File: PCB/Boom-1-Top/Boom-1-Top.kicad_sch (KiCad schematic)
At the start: 1029 parts, among them J1 DEBUG, J10 PIC_DEBUG, J11 PIC_DEBUG, J12 PIC_DEBUG, J13 PIC_DEBUG, J14 PIC_DEBUG, J15 USB_B_Micro, J16 SD_Card, J17 BT_DEBUG, J18 12V Supply, J19 3V3 Bypass, J2 MIDI IN, J20 5V Bypass, J21 Env +12V Supply, J22 Env -12V Supply, J23 OLEDConn, J24 FiltConn1PassThru, J25 LeftI2C0Test, J26 AudioOutConn, J27 FiltConn2PassThru, J28 FiltConn2PassThruPower, J29 LeftI2C1Test, J3 MIDI OUT, J30 LeftI2C2Test, J31 LeftI2C3Test, J32 RightI2C0Test, J33 RightI2C1Test, J34 RightI2C2Test, J35 RightI2C3Test, J36 SPIBus1Test, J37 Osc1Conn, J38 Osc2Conn, J39 SubNoiseConn, J4 PIC_DEBUG, J40 FiltConn2, J41 EnvGenConn2, J42 EnvGenConn1, J43 FXConn1, J44 FiltConn1, J45 FXConn2, J46 EnvGenConn3, J47 BTTestConn, J48 MIDITestConn, J49 I2CBus1TestConn, J5 PIC_DEBUG, J50 I2CBus2TestConn, J51 OLEDTestConn, J52 SDIOTestConn, J53 HapticEngine, J54 OLEDPowerTest, J6 PIC_DEBUG, J7 PIC_DEBUG, J8 PIC_DEBUG, J9 PIC_DEBUG, Q1 AO3401A, Q2 AO3401A, SW1 Osc1SawEncoder, SW10 SubToOsc2FiltEncoder, SW11 Osc1ToOsc2FiltEncoder, SW12 Osc1FiltFreqEncoder, SW13 Osc2FiltFreqEncoder, SW14 SubFiltFreqEncoder, SW15 OscFiltEnvAttackEncoder, SW16 SubFiltEnvAttackEncoder, SW17 Osc1FiltResEncoder, SW18 Osc2FiltResEncoder, SW19 SubFiltResEncoder, SW2 Osc1SqrEncoder, SW20 OscFiltEnvDecayEncoder, SW21 SubFiltEnvDecayEncoder, SW22 OscFiltEnvSustainEncoder, SW23 SubFiltEnvSustainEncoder, SW24 Osc1DriveEncoder, SW25 Osc2DistortionEncoder, SW26 OscFiltEnvReleaseEncoder, SW27 SubFiltEnvReleaseEncoder, SW28 FXWetDryEncoder, SW29 SubAmpEnvAttackEncoder, SW3 Rotary_Encoder, SW30 OscAmpEnvAttackEncoder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

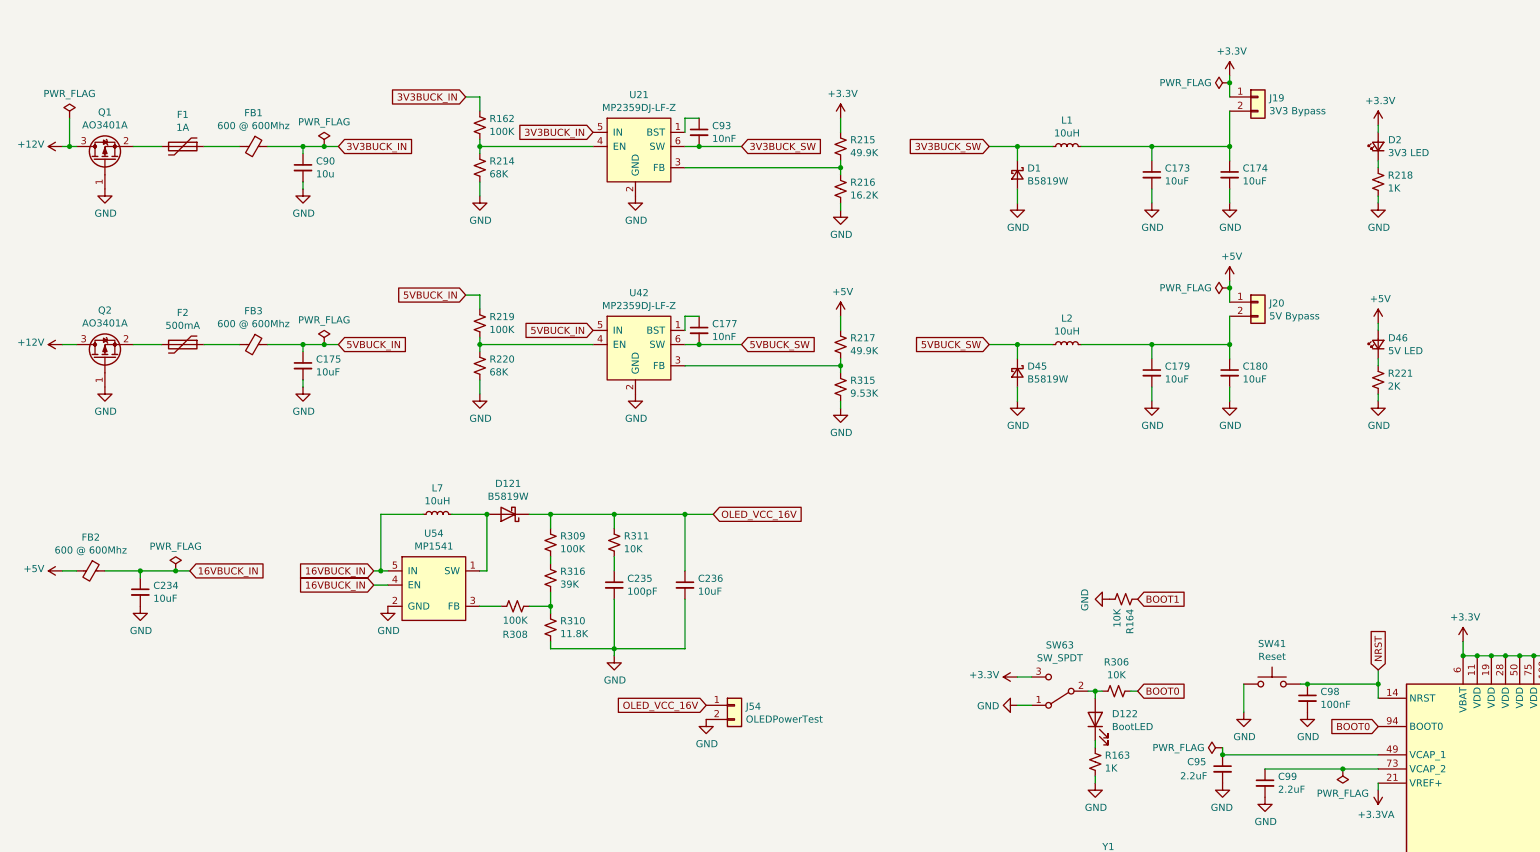
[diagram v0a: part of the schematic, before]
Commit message: Top: Power Rails
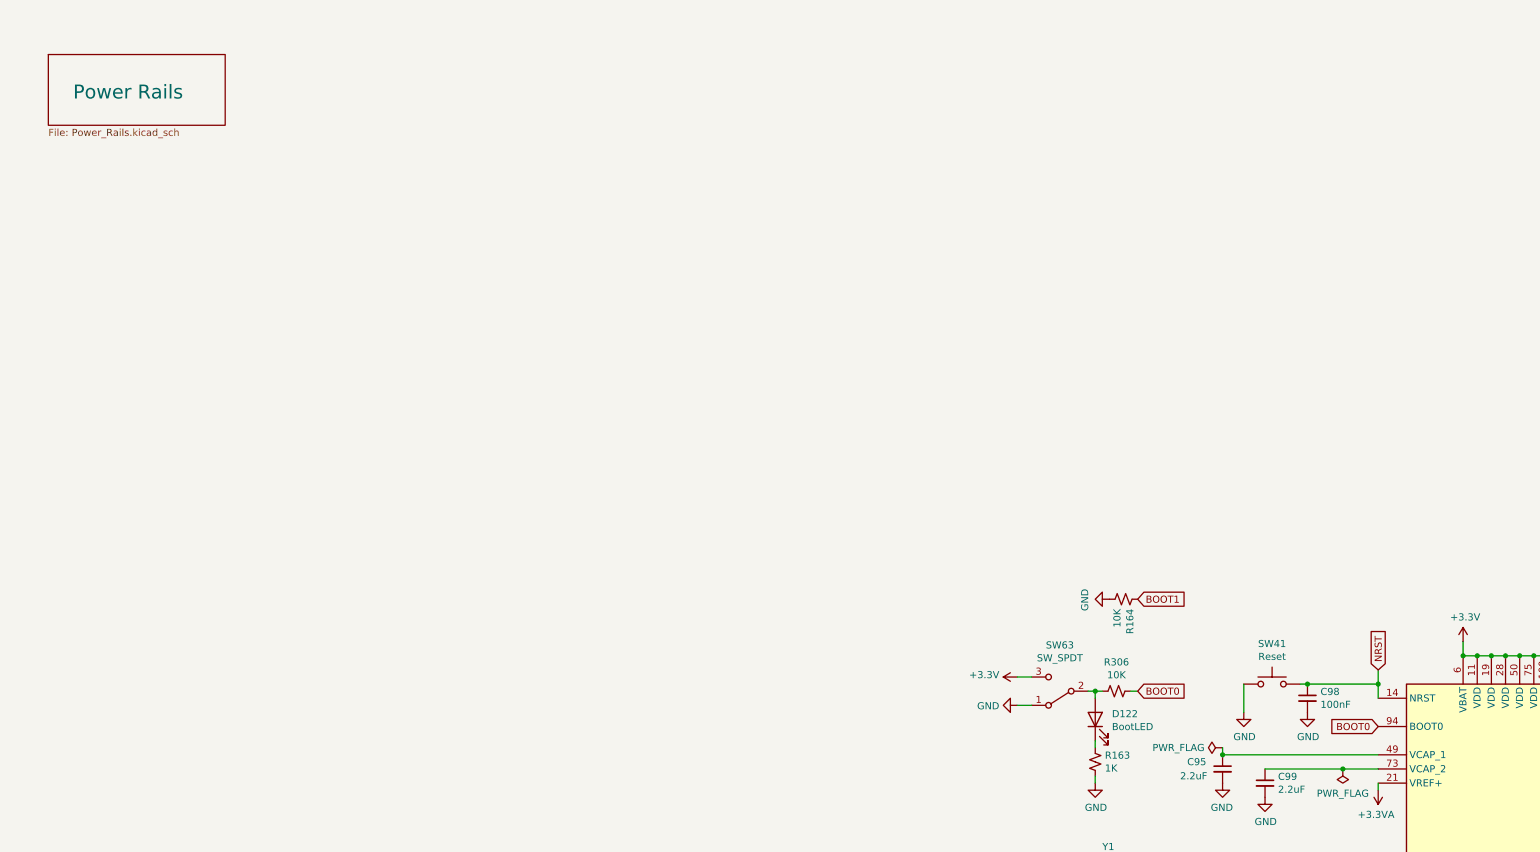
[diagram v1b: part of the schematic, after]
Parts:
- removed C173, C174, C175, C179, C180, C234, C236: 10uF, Capacitor_SMD:C_1206_3216Metric, symbol Device:C_Small
- removed C177, C93: 10nF, Capacitor_SMD:C_0805_2012Metric, symbol Device:C_Small
- removed C235: 100pF, Capacitor_SMD:C_0805_2012Metric, symbol Device:C_Small
- removed C90: 10u, Capacitor_SMD:C_1206_3216Metric, symbol Device:C_Small
- removed D1, D45: B5819W, Diode_SMD:D_SOD-123, symbol Device:D_Schottky_Small
- removed D121: B5819W, Diode_SMD:D_SOD-123, symbol Device:D_Schottky
- removed D2: 3V3 LED, LED_SMD:LED_0603_1608Metric, symbol Device:LED_Small
- removed D46: 5V LED, LED_SMD:LED_0603_1608Metric, symbol Device:LED_Small
- removed F1: 1A, Fuse:Fuse_1206_3216Metric, symbol Device:Polyfuse
- removed F2: 500mA, Fuse:Fuse_1206_3216Metric, symbol Device:Polyfuse
- removed FB1, FB2, FB3: 600 @ 600Mhz, Inductor_SMD:L_0805_2012Metric, symbol Device:Ferrite_Bead_Small
- removed J19: 3V3 Bypass, TerminalBlock:TerminalBlock_bornier-2_P5.08mm, symbol Connector_Generic:Conn_01x02
- removed J20: 5V Bypass, TerminalBlock:TerminalBlock_bornier-2_P5.08mm, symbol Connector_Generic:Conn_01x02
- removed J54: OLEDPowerTest, Connector_PinSocket_2.54mm:PinSocket_1x02_P2.54mm_Vertical, symbol Connector_Generic:Conn_01x02
- removed L1, L2, L7: 10uH, Inductor_SMD:L_Sunlord_MWSA0518_5.4x5.2mm, symbol Device:L_Small
- removed Q1, Q2: AO3401A, Package_TO_SOT_SMD:SOT-23, symbol Transistor_FET:AO3401A
- removed R162, R219, R308: 100K, Resistor_SMD:R_1206_3216Metric, symbol Device:R_Small_US
- removed R214, R220: 68K, Resistor_SMD:R_0603_1608Metric, symbol Device:R_Small_US
- removed R215, R217: 49.9K, Resistor_SMD:R_0603_1608Metric, symbol Device:R_Small_US
- removed R216: 16.2K, Resistor_SMD:R_0603_1608Metric, symbol Device:R_Small_US
- removed R218: 1K, Resistor_SMD:R_0603_1608Metric, symbol Device:R_Small_US
- removed R221: 2K, Resistor_SMD:R_0603_1608Metric, symbol Device:R_Small_US
- removed R309: 100K, Resistor_SMD:R_0805_2012Metric, symbol Device:R_Small_US
- removed R310: 11.8K, Resistor_SMD:R_1206_3216Metric, symbol Device:R_Small_US
- removed R311: 10K, Resistor_SMD:R_1206_3216Metric, symbol Device:R_Small_US
- removed R315: 9.53K, Resistor_SMD:R_0603_1608Metric, symbol Device:R_Small_US
- removed R316: 39K, Resistor_SMD:R_0805_2012Metric, symbol Device:R_Small_US
- removed U21, U42: MP2359DJ-LF-Z, Package_TO_SOT_SMD:SOT-23-6, symbol MP2359DJ:MP2359DJ-LF-Z
- removed U54: MP1541, Package_TO_SOT_SMD:TSOT-23-5, symbol MP1541:MP1541
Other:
- added sheet Power Rails (Power_Rails.kicad_sch)

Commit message: Top: Mounting
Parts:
- removed H1, H10, H11, H12, H2, H3, H4, H5, H6, H8: MountingHole_Pad, MountingHole:MountingHole_2.2mm_M2_Pad, symbol Mechanical:MountingHole_Pad
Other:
- added sheet Mounting (Mounting.kicad_sch)

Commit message: Top: SD IO
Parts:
- removed J16: SD_Card, Connector_Card:SD_Kyocera_145638009211859+, symbol Connector:SD_Card
- removed J52: SDIOTestConn, Connector_PinHeader_2.54mm:PinHeader_2x06_P2.54mm_Vertical, symbol Connector_Generic:Conn_02x06_Odd_Even
- removed R206, R207, R208, R209, R210: 47K, Resistor_SMD:R_0603_1608Metric, symbol Device:R_Small_US
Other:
- added sheet SD IO (SD_IO.kicad_sch)

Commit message: Top [WIP]: Rotary Encoders
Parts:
- removed C1, C10, C11, C12, C13, C139, C14, C140, C19, C2, C20, C21, C22, C23, C24, C25, C26, C27, C28, C29, C3, C30, C31, C32, C33, C34, C35, C36, C37, C38, C39, C4, C40, C41, C42, C43, C44, C45, C46, C47, C48, C49, C5, C50, C51, C52, C53, C54, C55, C56, C57, C58, C59, C6, C60, C61, C62, C63, C64, C65, C66, C67, C68, C69, C7, C70, C71, C72, C73, C74, C75, C76, C77, C78, C79, C8, C80, C9: 47nF, Capacitor_SMD:C_0603_1608Metric, symbol Device:C_Small
- removed C117, C118, C119, C120, C121, C122, C123, C124, C125, C126, C127, C128, C129, C130, C131, C132, C133, C134, C135, C136, C137, C138: 100nF, Capacitor_SMD:C_0402_1005Metric, symbol Device:C_Small
- removed D11, D14, D15, D17, D19, D23, D24, D25, D5, D6, D7, D9: B5819W, Diode_SMD:D_SOD-123, symbol Device:D_Small
- removed D12: Osc1SqrMixLED, LED_SMD:LED_0603_1608Metric, symbol Device:LED
- removed D13: Osc1SqrPWMLED, LED_SMD:LED_0603_1608Metric, symbol Device:LED
- removed D16: Osc2SqrMixLED, LED_SMD:LED_0603_1608Metric, symbol Device:LED
- removed D18: Osc2SqrPWMLED, LED_SMD:LED_0603_1608Metric, symbol Device:LED
- removed D43: OscFiltEnv1LED, LED_SMD:LED_0603_1608Metric, symbol Device:LED
- removed D44: OscFiltEnv2LED, LED_SMD:LED_0603_1608Metric, symbol Device:LED
- removed D52: OscFiltSusLED, LED_SMD:LED_0603_1608Metric, symbol Device:LED
- removed D53: OscFiltAmtLED, LED_SMD:LED_0603_1608Metric, symbol Device:LED
- removed D54: SubFilt1LED, LED_SMD:LED_0603_1608Metric, symbol Device:LED
- removed D55: SubFilt2LED, LED_SMD:LED_0603_1608Metric, symbol Device:LED
- removed D58: SubFiltSusLED, LED_SMD:LED_0603_1608Metric, symbol Device:LED
- removed D59: SubFiltAmtLED, LED_SMD:LED_0603_1608Metric, symbol Device:LED
- removed D62: OscAmpEnvSusLED, LED_SMD:LED_0603_1608Metric, symbol Device:LED
- removed D63: OscAmpEnvAmtLED, LED_SMD:LED_0603_1608Metric, symbol Device:LED
- removed D64: SubAmpEnvSusLED, LED_SMD:LED_0603_1608Metric, symbol Device:LED
- removed D65: SubAmpEnvAmtLED, LED_SMD:LED_0603_1608Metric, symbol Device:LED
- removed J10, J11, J12, J13, J14, J4, J5, J6, J7, J8, J9: PIC_DEBUG, Connector_PinHeader_1.27mm:PinHeader_1x05_P1.27mm_Vertical, symbol Connector_Generic:Conn_01x05
- removed R1, R10, R100, R101, R102, R103, R104, R105, R106, R107, R108, R109, R11, R110, R111, R112, R113, R114, R115, R116, R117, R118, R119, R12, R120, R121, R122, R123, R124, R125, R126, R127, R128, R129, R13, R130, R131, R132, R133, R134, R135, R136, R137, R138, R139, R14, R140, R141, R142, R143, R144, R145, R146, R147, R148, R149, R15, R150, R151, R152, R153, R154, R155, R156, R157, R158, R159, R16, R160, R17, R18, R183, R184, R185, R186, R2, R21, R22, R23, R24, R27, R28, R29, R3, R30, R31, R32, R37, R38, R39, R4, R40, R41, R42, R43, R44, R45, R46, R47, R48, R49, R5, R50, R51, R52, R53, R54, R55, R56, R57, R58, R59, R6, R60, R61, R62, R63, R64, R65, R66, R67, R68, R69, R7, R70, R71, R72, R73, R74, R75, R76, R77, R78, R79, R8, R80, R81, R82, R83, R84, R85, R86, R87, R88, R89, R9, R90, R91, R92, R93, R94, R95, R96, R97, R98, R99: 10K, Resistor_SMD:R_0402_1005Metric, symbol Device:R_Small_US
- removed R172, R173, R174, R175, R176, R177, R178, R179, R180, R181, R182: 10K, Resistor_SMD:R_0603_1608Metric, symbol Device:R_Small_US
- removed R276, R277, R278, R279, R280, R281, R282, R283, R284, R285, R286, R287, R288, R289, R290, R291: 42R2, Resistor_SMD:R_0603_1608Metric, symbol Device:R_Small_US
- removed SW1: Osc1SawEncoder, PEC11R:PEC11R-4x15F-N0024, symbol Device:Rotary_Encoder
- removed SW10: SubToOsc2FiltEncoder, PEC11R:PEC11R-4x15F-N0024, symbol Device:Rotary_Encoder
- removed SW11: Osc1ToOsc2FiltEncoder, PEC11R:PEC11R-4x15F-N0024, symbol Device:Rotary_Encoder
- removed SW12: Osc1FiltFreqEncoder, PEC11R:PEC11R-4x15F-N0024, symbol Device:Rotary_Encoder
- removed SW13: Osc2FiltFreqEncoder, PEC11R:PEC11R-4x15F-N0024, symbol Device:Rotary_Encoder
- removed SW14: SubFiltFreqEncoder, PEC11R:PEC11R-4x15F-N0024, symbol Device:Rotary_Encoder
- removed SW15: OscFiltEnvAttackEncoder, PEC11R:PEC11R-4x15F-S0024, symbol Device:Rotary_Encoder_Switch
- removed SW16: SubFiltEnvAttackEncoder, PEC11R:PEC11R-4x15F-S0024, symbol Device:Rotary_Encoder_Switch
- removed SW17: Osc1FiltResEncoder, PEC11R:PEC11R-4x15F-N0024, symbol Device:Rotary_Encoder
- removed SW18: Osc2FiltResEncoder, PEC11R:PEC11R-4x15F-N0024, symbol Device:Rotary_Encoder
- removed SW19: SubFiltResEncoder, PEC11R:PEC11R-4x15F-N0024, symbol Device:Rotary_Encoder
- removed SW2: Osc1SqrEncoder, PEC11R:PEC11R-4x15F-S0024, symbol Device:Rotary_Encoder_Switch
- removed SW20: OscFiltEnvDecayEncoder, PEC11R:PEC11R-4x15F-N0024, symbol Device:Rotary_Encoder
- removed SW21: SubFiltEnvDecayEncoder, PEC11R:PEC11R-4x15F-N0024, symbol Device:Rotary_Encoder
- removed SW22: OscFiltEnvSustainEncoder, PEC11R:PEC11R-4x15F-S0024, symbol Device:Rotary_Encoder_Switch
- removed SW23: SubFiltEnvSustainEncoder, PEC11R:PEC11R-4x15F-S0024, symbol Device:Rotary_Encoder_Switch
- removed SW24: Osc1DriveEncoder, PEC11R:PEC11R-4x15F-N0024, symbol Device:Rotary_Encoder
- removed SW25: Osc2DistortionEncoder, PEC11R:PEC11R-4x15F-N0024, symbol Device:Rotary_Encoder
- removed SW26: OscFiltEnvReleaseEncoder, PEC11R:PEC11R-4x15F-N0024, symbol Device:Rotary_Encoder
- removed SW27: SubFiltEnvReleaseEncoder, PEC11R:PEC11R-4x15F-N0024, symbol Device:Rotary_Encoder
- removed SW28: FXWetDryEncoder, PEC11R:PEC11R-4x15F-S0024, symbol Device:Rotary_Encoder_Switch
- removed SW29: SubAmpEnvAttackEncoder, PEC11R:PEC11R-4x15F-N0024, symbol Device:Rotary_Encoder
- removed SW3, SW5: Rotary_Encoder, PEC11R:PEC11R-4x15F-N0024, symbol Device:Rotary_Encoder
- removed SW30: OscAmpEnvAttackEncoder, PEC11R:PEC11R-4x15F-N0024, symbol Device:Rotary_Encoder
- removed SW31: FXControl1Encoder, PEC11R:PEC11R-4x15F-N0024, symbol Device:Rotary_Encoder
- removed SW32: SubAmpEnvDecayEncoder, PEC11R:PEC11R-4x15F-N0024, symbol Device:Rotary_Encoder
- removed SW33: OscAmpEnvDecayEncoder, PEC11R:PEC11R-4x15F-N0024, symbol Device:Rotary_Encoder
- removed SW34: FXControl2Encoder, PEC11R:PEC11R-4x15F-N0024, symbol Device:Rotary_Encoder
- removed SW35: SubAmpEnvSustainEncoder, PEC11R:PEC11R-4x15F-S0024, symbol Device:Rotary_Encoder_Switch
- removed SW36: OscAmpEnvSustainEncoder, PEC11R:PEC11R-4x15F-S0024, symbol Device:Rotary_Encoder_Switch
- removed SW37: FXControl3Encoder, PEC11R:PEC11R-4x15F-N0024, symbol Device:Rotary_Encoder
- removed SW38: FXFeedbackEncoder, PEC11R:PEC11R-4x15F-N0024, symbol Device:Rotary_Encoder
- removed SW39: SubAmpEnvReleaseEncoder, PEC11R:PEC11R-4x15F-N0024, symbol Device:Rotary_Encoder
- removed SW4: Rotary_Encoder_Switch, PEC11R:PEC11R-4x15F-S0024, symbol Device:Rotary_Encoder_Switch
- removed SW40: OscAmpEnvReleaseEncoder, PEC11R:PEC11R-4x15F-N0024, symbol Device:Rotary_Encoder
- removed SW43: Reset, PTS636:PTS636, symbol Switch:SW_Push
- removed SW53: Osc1TuneEncoder, PEC11R:PEC11R-4x15F-S0024, symbol Device:Rotary_Encoder_Switch
- removed SW6: SubToSubFiltEncoder, PEC11R:PEC11R-4x15F-N0024, symbol Device:Rotary_Encoder
- removed SW7: SubNoiseEncoder, PEC11R:PEC11R-4x15F-N0024, symbol Device:Rotary_Encoder
- removed U11, U12, U13, U14, U15, U16, U17, U18, U19, U2, U20: PIC18F26Q43, Package_SO:SSOP-28_5.3x10.2mm_P0.65mm, symbol PIC18F26Q43:PIC18F26Q43
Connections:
- no-connect marks 334 -> 262
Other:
- added sheet Rotary Encoders (Rotary_Encoders.kicad_sch)
- note removed: "GND"
- note removed: "LEFT0:000"
- note removed: "LEFT0:001"
- note removed: "LEFT0:010"
- note removed: "LEFT0:011"
- note removed: "LEFT0:100"
- note removed: "LEFT2:000"
- note removed: "LEFT2:001"
- note removed: "LEFT3:000"
- note removed: "PGC"
- note removed: "PGD"
- note removed: "RIGHT0:000"
- note removed: "RIGHT1:000"
- note removed: "RIGHT1:001"
- note removed: "VDD"
- note removed: "VPP/MCLR"

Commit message: Top: more splitting up done, still [WIP]
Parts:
- removed C100, C101, C141, C143, C145, C147, C149, C15, C150, C151, C153, C154, C155, C156, C157, C158, C160, C162, C164, C165, C168, C169, C17, C171, C172, C187, C195, C203, C209, C213, C215, C216, C217, C218, C219, C221, C222, C224, C225, C226, C227, C229, C81, C83, C87, C89, C91, C92, C94, C96, C98: 100nF, Capacitor_SMD:C_0402_1005Metric, symbol Device:C_Small
- removed C102, C82, C84, C97: 10uF, Capacitor_SMD:C_0603_1608Metric, symbol Device:CP_Small
- removed C142, C144, C146, C148, C152, C159, C16, C161, C163, C166, C167, C18, C188, C196, C204, C210, C214, C220, C223: 1uF, Capacitor_SMD:C_0402_1005Metric, symbol Device:C_Small
- removed C170: 10nF, Capacitor_SMD:C_0402_1005Metric, symbol Device:C_Small
- removed C228, C86: 4.7uF, Capacitor_SMD:C_0805_2012Metric, symbol Device:C_Small
- removed C85, C88: 12pF, Capacitor_SMD:C_0402_1005Metric, symbol Device:C_Small
- removed C95, C99: 2.2uF, Capacitor_SMD:C_0603_1608Metric, symbol Device:C_Small
- removed D100: OscTuneLED11, LED_SMD:LED_0603_1608Metric, symbol Device:LED
- removed D101: OscTuneLED12, LED_SMD:LED_0603_1608Metric, symbol Device:LED
- removed D102: OscTuneLED13, LED_SMD:LED_0603_1608Metric, symbol Device:LED
- removed D103: Osc2FiltLED1, fm-b2020rgba-hg:FM-B2020RGBA-HG, symbol fm-b2020rgba-hg:FM-B2020RGBA-HG
- removed D104: Osc2FiltLED2, fm-b2020rgba-hg:FM-B2020RGBA-HG, symbol fm-b2020rgba-hg:FM-B2020RGBA-HG
- removed D105, D106, D109, D110, D68, D69, D72, D73, D74, D75, D80, D81, D82, D83, D84, D85, D88, D89: StepLED, fm-b2020rgba-hg:FM-B2020RGBA-HG, symbol fm-b2020rgba-hg:FM-B2020RGBA-HG
- removed D107: SubFiltLED1, fm-b2020rgba-hg:FM-B2020RGBA-HG, symbol fm-b2020rgba-hg:FM-B2020RGBA-HG
- removed D108: SubFiltLED2, fm-b2020rgba-hg:FM-B2020RGBA-HG, symbol fm-b2020rgba-hg:FM-B2020RGBA-HG
- removed D111: OscFiltEnvLED1, fm-b2020rgba-hg:FM-B2020RGBA-HG, symbol fm-b2020rgba-hg:FM-B2020RGBA-HG
- removed D112: OscFiltEnvLED2, fm-b2020rgba-hg:FM-B2020RGBA-HG, symbol fm-b2020rgba-hg:FM-B2020RGBA-HG
- removed D113: OscFiltEnvLED3, fm-b2020rgba-hg:FM-B2020RGBA-HG, symbol fm-b2020rgba-hg:FM-B2020RGBA-HG
- removed D114, D115, D116, D120: PageLED, LED_SMD:LED_0603_1608Metric, symbol Device:LED
- removed D117: SubFiltEnvLED1, fm-b2020rgba-hg:FM-B2020RGBA-HG, symbol fm-b2020rgba-hg:FM-B2020RGBA-HG
- removed D118: SubFiltEnvLED2, fm-b2020rgba-hg:FM-B2020RGBA-HG, symbol fm-b2020rgba-hg:FM-B2020RGBA-HG
- removed D119: SubFiltEnvLED3, fm-b2020rgba-hg:FM-B2020RGBA-HG, symbol fm-b2020rgba-hg:FM-B2020RGBA-HG
- removed D122: BootLED, LED_SMD:LED_0603_1608Metric, symbol Device:LED
- removed D123: Osc1ResLED1, fm-b2020rgba-hg:FM-B2020RGBA-HG, symbol fm-b2020rgba-hg:FM-B2020RGBA-HG
- removed D124: Osc1ResLED2, fm-b2020rgba-hg:FM-B2020RGBA-HG, symbol fm-b2020rgba-hg:FM-B2020RGBA-HG
- removed D127: Osc2ResLED1, fm-b2020rgba-hg:FM-B2020RGBA-HG, symbol fm-b2020rgba-hg:FM-B2020RGBA-HG
- removed D128: Osc2ResLED2, fm-b2020rgba-hg:FM-B2020RGBA-HG, symbol fm-b2020rgba-hg:FM-B2020RGBA-HG
- removed D131: SubResLED1, fm-b2020rgba-hg:FM-B2020RGBA-HG, symbol fm-b2020rgba-hg:FM-B2020RGBA-HG
- removed D132: SubResLED2, fm-b2020rgba-hg:FM-B2020RGBA-HG, symbol fm-b2020rgba-hg:FM-B2020RGBA-HG
- removed D133: SubResLED3, fm-b2020rgba-hg:FM-B2020RGBA-HG, symbol fm-b2020rgba-hg:FM-B2020RGBA-HG
- removed D134: SubResLED4, fm-b2020rgba-hg:FM-B2020RGBA-HG, symbol fm-b2020rgba-hg:FM-B2020RGBA-HG
- removed D135: SubResLED5, fm-b2020rgba-hg:FM-B2020RGBA-HG, symbol fm-b2020rgba-hg:FM-B2020RGBA-HG
- removed D136: SubResLED6, fm-b2020rgba-hg:FM-B2020RGBA-HG, symbol fm-b2020rgba-hg:FM-B2020RGBA-HG
- removed D137: SubResLED7, fm-b2020rgba-hg:FM-B2020RGBA-HG, symbol fm-b2020rgba-hg:FM-B2020RGBA-HG
- removed D144: Osc1DriveLED1, fm-b2020rgba-hg:FM-B2020RGBA-HG, symbol fm-b2020rgba-hg:FM-B2020RGBA-HG
- removed D145: Osc1DriveLED2, fm-b2020rgba-hg:FM-B2020RGBA-HG, symbol fm-b2020rgba-hg:FM-B2020RGBA-HG
- removed D147: Osc1DriveLED3, fm-b2020rgba-hg:FM-B2020RGBA-HG, symbol fm-b2020rgba-hg:FM-B2020RGBA-HG
- removed D148: Osc1DriveLED4, fm-b2020rgba-hg:FM-B2020RGBA-HG, symbol fm-b2020rgba-hg:FM-B2020RGBA-HG
- removed D152: Osc2DriveLED2, fm-b2020rgba-hg:FM-B2020RGBA-HG, symbol fm-b2020rgba-hg:FM-B2020RGBA-HG
- removed D153: Osc2DriveLED10, fm-b2020rgba-hg:FM-B2020RGBA-HG, symbol fm-b2020rgba-hg:FM-B2020RGBA-HG
- removed D154: Osc2DriveLED3, fm-b2020rgba-hg:FM-B2020RGBA-HG, symbol fm-b2020rgba-hg:FM-B2020RGBA-HG
- removed D159: Osc2DriveLED13, fm-b2020rgba-hg:FM-B2020RGBA-HG, symbol fm-b2020rgba-hg:FM-B2020RGBA-HG
- removed D162: OscAmpLED1, fm-b2020rgba-hg:FM-B2020RGBA-HG, symbol fm-b2020rgba-hg:FM-B2020RGBA-HG
- removed D163: OscAmpLED2, fm-b2020rgba-hg:FM-B2020RGBA-HG, symbol fm-b2020rgba-hg:FM-B2020RGBA-HG
- removed D164: OscAmpLED3, fm-b2020rgba-hg:FM-B2020RGBA-HG, symbol fm-b2020rgba-hg:FM-B2020RGBA-HG
- removed D165: SubAmpLED1, fm-b2020rgba-hg:FM-B2020RGBA-HG, symbol fm-b2020rgba-hg:FM-B2020RGBA-HG
- removed D166: SubAmpLED2, fm-b2020rgba-hg:FM-B2020RGBA-HG, symbol fm-b2020rgba-hg:FM-B2020RGBA-HG
- removed D167: SubAmpLED3, fm-b2020rgba-hg:FM-B2020RGBA-HG, symbol fm-b2020rgba-hg:FM-B2020RGBA-HG
- removed D168: SubAmpLED4, fm-b2020rgba-hg:FM-B2020RGBA-HG, symbol fm-b2020rgba-hg:FM-B2020RGBA-HG
- removed D169: SubvAmpLED5, fm-b2020rgba-hg:FM-B2020RGBA-HG, symbol fm-b2020rgba-hg:FM-B2020RGBA-HG
- removed D173: OscAmpLED4, fm-b2020rgba-hg:FM-B2020RGBA-HG, symbol fm-b2020rgba-hg:FM-B2020RGBA-HG
- removed D174: OscAmpLED5, fm-b2020rgba-hg:FM-B2020RGBA-HG, symbol fm-b2020rgba-hg:FM-B2020RGBA-HG
- removed D175: FXDryLED1, fm-b2020rgba-hg:FM-B2020RGBA-HG, symbol fm-b2020rgba-hg:FM-B2020RGBA-HG
- removed D176: FXDryLED2, fm-b2020rgba-hg:FM-B2020RGBA-HG, symbol fm-b2020rgba-hg:FM-B2020RGBA-HG
- removed D177: FXDryLED3, fm-b2020rgba-hg:FM-B2020RGBA-HG, symbol fm-b2020rgba-hg:FM-B2020RGBA-HG
- removed D178: FXDryLED4, fm-b2020rgba-hg:FM-B2020RGBA-HG, symbol fm-b2020rgba-hg:FM-B2020RGBA-HG
- removed D179: FXDryLED5, fm-b2020rgba-hg:FM-B2020RGBA-HG, symbol fm-b2020rgba-hg:FM-B2020RGBA-HG
- removed D180: FXDryLED6, fm-b2020rgba-hg:FM-B2020RGBA-HG, symbol fm-b2020rgba-hg:FM-B2020RGBA-HG
- removed D181: FXDryLED7, fm-b2020rgba-hg:FM-B2020RGBA-HG, symbol fm-b2020rgba-hg:FM-B2020RGBA-HG
- removed D182: FXDryLED8, fm-b2020rgba-hg:FM-B2020RGBA-HG, symbol fm-b2020rgba-hg:FM-B2020RGBA-HG
- removed D183: FXDryLED9, fm-b2020rgba-hg:FM-B2020RGBA-HG, symbol fm-b2020rgba-hg:FM-B2020RGBA-HG
- removed D184: FXDryLED10, fm-b2020rgba-hg:FM-B2020RGBA-HG, symbol fm-b2020rgba-hg:FM-B2020RGBA-HG
- removed D190: FXWetLED1, fm-b2020rgba-hg:FM-B2020RGBA-HG, symbol fm-b2020rgba-hg:FM-B2020RGBA-HG
- removed D193: FXWetLED4, fm-b2020rgba-hg:FM-B2020RGBA-HG, symbol fm-b2020rgba-hg:FM-B2020RGBA-HG
- removed D196: FXWetLED7, fm-b2020rgba-hg:FM-B2020RGBA-HG, symbol fm-b2020rgba-hg:FM-B2020RGBA-HG
- removed D197: FXWetLED8, fm-b2020rgba-hg:FM-B2020RGBA-HG, symbol fm-b2020rgba-hg:FM-B2020RGBA-HG
- removed D198: FXWetLED9, fm-b2020rgba-hg:FM-B2020RGBA-HG, symbol fm-b2020rgba-hg:FM-B2020RGBA-HG
- removed D199: FXWetLED10, fm-b2020rgba-hg:FM-B2020RGBA-HG, symbol fm-b2020rgba-hg:FM-B2020RGBA-HG
- removed D20: Osc1SawLED2, fm-b2020rgba-hg:FM-B2020RGBA-HG, symbol fm-b2020rgba-hg:FM-B2020RGBA-HG
- removed D202: FXFbLED1, fm-b2020rgba-hg:FM-B2020RGBA-HG, symbol fm-b2020rgba-hg:FM-B2020RGBA-HG
- removed D203: FXFbLED2, fm-b2020rgba-hg:FM-B2020RGBA-HG, symbol fm-b2020rgba-hg:FM-B2020RGBA-HG
- removed D205: FXFbLED3, fm-b2020rgba-hg:FM-B2020RGBA-HG, symbol fm-b2020rgba-hg:FM-B2020RGBA-HG
- removed D206: FXFbLED4, fm-b2020rgba-hg:FM-B2020RGBA-HG, symbol fm-b2020rgba-hg:FM-B2020RGBA-HG
- removed D207: FXFbLED5, fm-b2020rgba-hg:FM-B2020RGBA-HG, symbol fm-b2020rgba-hg:FM-B2020RGBA-HG
- removed D209: FXFbLED6, fm-b2020rgba-hg:FM-B2020RGBA-HG, symbol fm-b2020rgba-hg:FM-B2020RGBA-HG
- removed D21: Osc1SqrLED2, fm-b2020rgba-hg:FM-B2020RGBA-HG, symbol fm-b2020rgba-hg:FM-B2020RGBA-HG
- removed D210: FXFbLED7, fm-b2020rgba-hg:FM-B2020RGBA-HG, symbol fm-b2020rgba-hg:FM-B2020RGBA-HG
- removed D211: FXFbLED18, fm-b2020rgba-hg:FM-B2020RGBA-HG, symbol fm-b2020rgba-hg:FM-B2020RGBA-HG
- removed D218: OscFiltEnvAtkLED1, LED_SMD:LED_0603_1608Metric, symbol Device:LED
- removed D219: OscFiltEnvAtkLED2, LED_SMD:LED_0603_1608Metric, symbol Device:LED
- removed D22: Osc2SawLED2, fm-b2020rgba-hg:FM-B2020RGBA-HG, symbol fm-b2020rgba-hg:FM-B2020RGBA-HG
- removed D220: OscFiltEnvAtkLED3, LED_SMD:LED_0603_1608Metric, symbol Device:LED
- removed D221: OscFiltEnvAtkLED4, LED_SMD:LED_0603_1608Metric, symbol Device:LED
- removed D222: OscFiltEnvAtkLED5, LED_SMD:LED_0603_1608Metric, symbol Device:LED
- removed D223: OscFiltEnvAtkLED6, LED_SMD:LED_0603_1608Metric, symbol Device:LED
- removed D224: OscFiltEnvDcyLED1, LED_SMD:LED_0603_1608Metric, symbol Device:LED
- removed D225: OscFiltEnvDcyLED2, LED_SMD:LED_0603_1608Metric, symbol Device:LED
- removed D226: OscFiltEnvDcyLED3, LED_SMD:LED_0603_1608Metric, symbol Device:LED
- removed D227: OscFiltEnvDcyLED4, LED_SMD:LED_0603_1608Metric, symbol Device:LED
- removed D228: OscFiltEnvDcyLED5, LED_SMD:LED_0603_1608Metric, symbol Device:LED
- removed D229: OscFiltEnvDcyLED6, LED_SMD:LED_0603_1608Metric, symbol Device:LED
- removed D230: OscFiltEnvSusLED1, LED_SMD:LED_0603_1608Metric, symbol Device:LED
- removed D231: OscFiltEnvSusLED2, LED_SMD:LED_0603_1608Metric, symbol Device:LED
- removed D232: OscFiltEnvSusLED3, LED_SMD:LED_0603_1608Metric, symbol Device:LED
- removed D233: OscFiltEnvSusLED4, LED_SMD:LED_0603_1608Metric, symbol Device:LED
- removed D234: OscFiltEnvSusLED5, LED_SMD:LED_0603_1608Metric, symbol Device:LED
- removed D235: OscFiltEnvSusLED6, LED_SMD:LED_0603_1608Metric, symbol Device:LED
- removed D236: OscFiltEnvRelLED1, LED_SMD:LED_0603_1608Metric, symbol Device:LED
- removed D237: OscFiltEnvRelLED2, LED_SMD:LED_0603_1608Metric, symbol Device:LED
- removed D238: OscFiltEnvRelLED3, LED_SMD:LED_0603_1608Metric, symbol Device:LED
- removed D239: OscFiltEnvRelLED4, LED_SMD:LED_0603_1608Metric, symbol Device:LED
- removed D240: OscFiltEnvRelLED5, LED_SMD:LED_0603_1608Metric, symbol Device:LED
- removed D241: OscFiltEnvRelLED6, LED_SMD:LED_0603_1608Metric, symbol Device:LED
- removed D242: SubFiltEnvAtkLED1, LED_SMD:LED_0603_1608Metric, symbol Device:LED
- removed D243: SubFiltEnvAtkLED2, LED_SMD:LED_0603_1608Metric, symbol Device:LED
- removed D244: SubFiltEnvAtkLED3, LED_SMD:LED_0603_1608Metric, symbol Device:LED
- removed D245: SubFiltEnvAtkLED4, LED_SMD:LED_0603_1608Metric, symbol Device:LED
- removed D246: SubFiltEnvAtkLED5, LED_SMD:LED_0603_1608Metric, symbol Device:LED
- removed D247: SubFiltEnvAtkLED6, LED_SMD:LED_0603_1608Metric, symbol Device:LED
- removed D248: SubFiltEnvDcyLED1, LED_SMD:LED_0603_1608Metric, symbol Device:LED
- removed D249: SubFiltEnvDcyLED2, LED_SMD:LED_0603_1608Metric, symbol Device:LED
- removed D250: SubFiltEnvDcyLED3, LED_SMD:LED_0603_1608Metric, symbol Device:LED
- removed D251: SubFiltEnvDcyLED4, LED_SMD:LED_0603_1608Metric, symbol Device:LED
- removed D252: SubFiltEnvDcyLED5, LED_SMD:LED_0603_1608Metric, symbol Device:LED
- removed D253: SubFiltEnvDcyLED6, LED_SMD:LED_0603_1608Metric, symbol Device:LED
- removed D254: SubFiltEnvSusLED1, LED_SMD:LED_0603_1608Metric, symbol Device:LED
- removed D255: SubFiltEnvSusLED2, LED_SMD:LED_0603_1608Metric, symbol Device:LED
- removed D256: SubFiltEnvSusLED3, LED_SMD:LED_0603_1608Metric, symbol Device:LED
- removed D257: SubFiltEnvSusLED4, LED_SMD:LED_0603_1608Metric, symbol Device:LED
- removed D258: SubFiltEnvSusLED5, LED_SMD:LED_0603_1608Metric, symbol Device:LED
- removed D259: SubFiltEnvSusLED6, LED_SMD:LED_0603_1608Metric, symbol Device:LED
- removed D26: Osc2NoiseLED2, fm-b2020rgba-hg:FM-B2020RGBA-HG, symbol fm-b2020rgba-hg:FM-B2020RGBA-HG
- removed D260: SubFiltEnvRelLED1, LED_SMD:LED_0603_1608Metric, symbol Device:LED
- removed D261: SubFiltEnvRelLED2, LED_SMD:LED_0603_1608Metric, symbol Device:LED
- removed D262: SubFiltEnvRelLED3, LED_SMD:LED_0603_1608Metric, symbol Device:LED
- removed D263: SubFiltEnvRelLED4, LED_SMD:LED_0603_1608Metric, symbol Device:LED
- removed D264: SubFiltEnvRelLED5, LED_SMD:LED_0603_1608Metric, symbol Device:LED
- removed D265: SubFiltEnvRelLED6, LED_SMD:LED_0603_1608Metric, symbol Device:LED
- removed D266: OscAmpEnvAtkLED1, LED_SMD:LED_0603_1608Metric, symbol Device:LED
- removed D267: OscAmpEnvAtkLED2, LED_SMD:LED_0603_1608Metric, symbol Device:LED
- removed D268: OscAmpEnvAtkLED3, LED_SMD:LED_0603_1608Metric, symbol Device:LED
- removed D269: OscAmpEnvAtkLED4, LED_SMD:LED_0603_1608Metric, symbol Device:LED
- removed D27: SubOscLED2, fm-b2020rgba-hg:FM-B2020RGBA-HG, symbol fm-b2020rgba-hg:FM-B2020RGBA-HG
- removed D270: OscAmpEnvAtkLED5, LED_SMD:LED_0603_1608Metric, symbol Device:LED
- removed D271: OscAmpEnvAtkLED6, LED_SMD:LED_0603_1608Metric, symbol Device:LED
- removed D272: OscAmpEnvDcyLED1, LED_SMD:LED_0603_1608Metric, symbol Device:LED
- removed D273: OscAmpEnvDcyLED2, LED_SMD:LED_0603_1608Metric, symbol Device:LED
- removed D274: OscAmpEnvDcyLED3, LED_SMD:LED_0603_1608Metric, symbol Device:LED
- removed D275: OscAmpEnvDcyLED4, LED_SMD:LED_0603_1608Metric, symbol Device:LED
- removed D276: OscAmpEnvDcyLED5, LED_SMD:LED_0603_1608Metric, symbol Device:LED
- removed D277: OscAmpEnvDcyLED6, LED_SMD:LED_0603_1608Metric, symbol Device:LED
- removed D278: OscAmpEnvSusLED1, LED_SMD:LED_0603_1608Metric, symbol Device:LED
- removed D279: OscAmpEnvSusLED2, LED_SMD:LED_0603_1608Metric, symbol Device:LED
- removed D28: SubNoiseLED2, fm-b2020rgba-hg:FM-B2020RGBA-HG, symbol fm-b2020rgba-hg:FM-B2020RGBA-HG
- removed D280: OscAmpEnvSusLED3, LED_SMD:LED_0603_1608Metric, symbol Device:LED
- removed D281: OscAmpEnvSusLED4, LED_SMD:LED_0603_1608Metric, symbol Device:LED
- removed D282: OscAmpEnvSusLED5, LED_SMD:LED_0603_1608Metric, symbol Device:LED
- removed D283: OscAmpEnvSusLED6, LED_SMD:LED_0603_1608Metric, symbol Device:LED
- removed D284: OscAmpEnvRelLED1, LED_SMD:LED_0603_1608Metric, symbol Device:LED
- removed D285: OscAmpEnvRelLED2, LED_SMD:LED_0603_1608Metric, symbol Device:LED
- removed D286: OscAmpEnvRelLED3, LED_SMD:LED_0603_1608Metric, symbol Device:LED
- removed D287: OscAmpEnvRelLED4, LED_SMD:LED_0603_1608Metric, symbol Device:LED
- removed D288: OscAmpEnvRelLED5, LED_SMD:LED_0603_1608Metric, symbol Device:LED
- removed D289: OscAmpEnvRelLED6, LED_SMD:LED_0603_1608Metric, symbol Device:LED
- removed D29: Osc2SqrLED2, fm-b2020rgba-hg:FM-B2020RGBA-HG, symbol fm-b2020rgba-hg:FM-B2020RGBA-HG
- removed D290: SubAmpEnvAtkLED1, LED_SMD:LED_0603_1608Metric, symbol Device:LED
- removed D291: SubAmpEnvAtkLED2, LED_SMD:LED_0603_1608Metric, symbol Device:LED
- removed D292: SubAmpEnvAtkLED3, LED_SMD:LED_0603_1608Metric, symbol Device:LED
- removed D293: SubAmpEnvAtkLED4, LED_SMD:LED_0603_1608Metric, symbol Device:LED
- removed D294: SubAmpEnvAtkLED5, LED_SMD:LED_0603_1608Metric, symbol Device:LED
- removed D295: SubAmpEnvAtkLED6, LED_SMD:LED_0603_1608Metric, symbol Device:LED
- removed D296: SubAmpEnvDcyLED1, LED_SMD:LED_0603_1608Metric, symbol Device:LED
- removed D297: SubAmpEnvDcyLED2, LED_SMD:LED_0603_1608Metric, symbol Device:LED
- removed D298: SubAmpEnvDcyLED3, LED_SMD:LED_0603_1608Metric, symbol Device:LED
- removed D299: SubAmpEnvDcyLED4, LED_SMD:LED_0603_1608Metric, symbol Device:LED
- removed D3: 1N4148, Diode_SMD:D_SOD-123, symbol Device:D_Small
- removed D30: Osc1SawLED3, fm-b2020rgba-hg:FM-B2020RGBA-HG, symbol fm-b2020rgba-hg:FM-B2020RGBA-HG
- removed D300: SubAmpEnvDcyLED5, LED_SMD:LED_0603_1608Metric, symbol Device:LED
- removed D301: SubAmpEnvDcyLED6, LED_SMD:LED_0603_1608Metric, symbol Device:LED
- removed D302: SubAmpEnvSusLED1, LED_SMD:LED_0603_1608Metric, symbol Device:LED
- removed D303: SubAmpEnvSusLED2, LED_SMD:LED_0603_1608Metric, symbol Device:LED
- removed D304: SubAmpEnvSusLED3, LED_SMD:LED_0603_1608Metric, symbol Device:LED
- removed D305: SubAmpEnvSusLED4, LED_SMD:LED_0603_1608Metric, symbol Device:LED
- removed D306: SubAmpEnvSusLED5, LED_SMD:LED_0603_1608Metric, symbol Device:LED
- removed D307: SubAmpEnvSusLED6, LED_SMD:LED_0603_1608Metric, symbol Device:LED
- removed D308: SubAmpEnvRelLED1, LED_SMD:LED_0603_1608Metric, symbol Device:LED
- removed D309: SubAmpEnvRelLED2, LED_SMD:LED_0603_1608Metric, symbol Device:LED
- removed D31: Osc1SqrLED3, fm-b2020rgba-hg:FM-B2020RGBA-HG, symbol fm-b2020rgba-hg:FM-B2020RGBA-HG
- removed D310: SubAmpEnvRelLED3, LED_SMD:LED_0603_1608Metric, symbol Device:LED
- removed D311: SubAmpEnvRelLED4, LED_SMD:LED_0603_1608Metric, symbol Device:LED
- removed D312: SubAmpEnvRelLED5, LED_SMD:LED_0603_1608Metric, symbol Device:LED
- removed D313: SubAmpEnvRelLED6, LED_SMD:LED_0603_1608Metric, symbol Device:LED
- removed D315: Osc2DriveLED6, fm-b2020rgba-hg:FM-B2020RGBA-HG, symbol fm-b2020rgba-hg:FM-B2020RGBA-HG
- removed D316: Osc2DriveLED7, fm-b2020rgba-hg:FM-B2020RGBA-HG, symbol fm-b2020rgba-hg:FM-B2020RGBA-HG
- removed D317: Osc2DriveLED8, fm-b2020rgba-hg:FM-B2020RGBA-HG, symbol fm-b2020rgba-hg:FM-B2020RGBA-HG
- removed D32: Osc2SawLED3, fm-b2020rgba-hg:FM-B2020RGBA-HG, symbol fm-b2020rgba-hg:FM-B2020RGBA-HG
- removed D320: Osc2DriveLED9, fm-b2020rgba-hg:FM-B2020RGBA-HG, symbol fm-b2020rgba-hg:FM-B2020RGBA-HG
- removed D326: FXWetLED13, fm-b2020rgba-hg:FM-B2020RGBA-HG, symbol fm-b2020rgba-hg:FM-B2020RGBA-HG
- removed D33: Osc2NoiseLED3, fm-b2020rgba-hg:FM-B2020RGBA-HG, symbol fm-b2020rgba-hg:FM-B2020RGBA-HG
- removed D34: SubOscLED3, fm-b2020rgba-hg:FM-B2020RGBA-HG, symbol fm-b2020rgba-hg:FM-B2020RGBA-HG
- removed D35: SubNoiseLED3, fm-b2020rgba-hg:FM-B2020RGBA-HG, symbol fm-b2020rgba-hg:FM-B2020RGBA-HG
- removed D36: Osc2MixLED, fm-b2020rgba-hg:FM-B2020RGBA-HG, symbol fm-b2020rgba-hg:FM-B2020RGBA-HG
- removed D37: Osc1MixLED1, fm-b2020rgba-hg:FM-B2020RGBA-HG, symbol fm-b2020rgba-hg:FM-B2020RGBA-HG
- removed D38: SubNoiseMixLED1, fm-b2020rgba-hg:FM-B2020RGBA-HG, symbol fm-b2020rgba-hg:FM-B2020RGBA-HG
- removed D39: Osc1MixLED2, fm-b2020rgba-hg:FM-B2020RGBA-HG, symbol fm-b2020rgba-hg:FM-B2020RGBA-HG
- removed D4: FXDryLED11, fm-b2020rgba-hg:FM-B2020RGBA-HG, symbol fm-b2020rgba-hg:FM-B2020RGBA-HG
- removed D40: Osc1MixLED3, fm-b2020rgba-hg:FM-B2020RGBA-HG, symbol fm-b2020rgba-hg:FM-B2020RGBA-HG
- removed D41: Osc1MixLED4, fm-b2020rgba-hg:FM-B2020RGBA-HG, symbol fm-b2020rgba-hg:FM-B2020RGBA-HG
- removed D42: Osc1MixLED5, fm-b2020rgba-hg:FM-B2020RGBA-HG, symbol fm-b2020rgba-hg:FM-B2020RGBA-HG
- removed D47: Osc2MixLED1, fm-b2020rgba-hg:FM-B2020RGBA-HG, symbol fm-b2020rgba-hg:FM-B2020RGBA-HG
- removed D48: Osc2MixLED2, fm-b2020rgba-hg:FM-B2020RGBA-HG, symbol fm-b2020rgba-hg:FM-B2020RGBA-HG
- removed D49: Osc2MixLED3, fm-b2020rgba-hg:FM-B2020RGBA-HG, symbol fm-b2020rgba-hg:FM-B2020RGBA-HG
- removed D50: Osc2MixLED4, fm-b2020rgba-hg:FM-B2020RGBA-HG, symbol fm-b2020rgba-hg:FM-B2020RGBA-HG
- removed D51: Osc2MixLED5, fm-b2020rgba-hg:FM-B2020RGBA-HG, symbol fm-b2020rgba-hg:FM-B2020RGBA-HG
- removed D56: Osc1ToOsc2LED1, fm-b2020rgba-hg:FM-B2020RGBA-HG, symbol fm-b2020rgba-hg:FM-B2020RGBA-HG
- removed D57: Osc1ToOsc2LED2, fm-b2020rgba-hg:FM-B2020RGBA-HG, symbol fm-b2020rgba-hg:FM-B2020RGBA-HG
- removed D60: Osc1ToOsc2LED5, fm-b2020rgba-hg:FM-B2020RGBA-HG, symbol fm-b2020rgba-hg:FM-B2020RGBA-HG
- removed D61: Osc1ToOsc2ED6, fm-b2020rgba-hg:FM-B2020RGBA-HG, symbol fm-b2020rgba-hg:FM-B2020RGBA-HG
- removed D66: SubToOsc2LED1, fm-b2020rgba-hg:FM-B2020RGBA-HG, symbol fm-b2020rgba-hg:FM-B2020RGBA-HG
- removed D67: SubToOsc2LED2, fm-b2020rgba-hg:FM-B2020RGBA-HG, symbol fm-b2020rgba-hg:FM-B2020RGBA-HG
- removed D70: SubToOsc2LED5, fm-b2020rgba-hg:FM-B2020RGBA-HG, symbol fm-b2020rgba-hg:FM-B2020RGBA-HG
- removed D71: SubToOsc2ED6, fm-b2020rgba-hg:FM-B2020RGBA-HG, symbol fm-b2020rgba-hg:FM-B2020RGBA-HG
- removed D76: SubMixLED1, fm-b2020rgba-hg:FM-B2020RGBA-HG, symbol fm-b2020rgba-hg:FM-B2020RGBA-HG
- removed D77: SubMixLED2, fm-b2020rgba-hg:FM-B2020RGBA-HG, symbol fm-b2020rgba-hg:FM-B2020RGBA-HG
- removed D78: SubMixLED3, fm-b2020rgba-hg:FM-B2020RGBA-HG, symbol fm-b2020rgba-hg:FM-B2020RGBA-HG
- removed D79: SubMixLED4, fm-b2020rgba-hg:FM-B2020RGBA-HG, symbol fm-b2020rgba-hg:FM-B2020RGBA-HG
- removed D86: Osc1FiltLED1, fm-b2020rgba-hg:FM-B2020RGBA-HG, symbol fm-b2020rgba-hg:FM-B2020RGBA-HG
- removed D87: Osc1FiltLED2, fm-b2020rgba-hg:FM-B2020RGBA-HG, symbol fm-b2020rgba-hg:FM-B2020RGBA-HG
- removed D90: OscTuneLED1, LED_SMD:LED_0603_1608Metric, symbol Device:LED
- removed D91: OscTuneLED2, LED_SMD:LED_0603_1608Metric, symbol Device:LED
- removed D92: OscTuneLED3, LED_SMD:LED_0603_1608Metric, symbol Device:LED
- removed D93: OscTuneLED4, LED_SMD:LED_0603_1608Metric, symbol Device:LED
- removed D94: OscTuneLED5, LED_SMD:LED_0603_1608Metric, symbol Device:LED
- removed D95: OscTuneLED6, LED_SMD:LED_0603_1608Metric, symbol Device:LED
- removed D96: OscTuneLED7, LED_SMD:LED_0603_1608Metric, symbol Device:LED
- removed D97: OscTuneLED8, LED_SMD:LED_0603_1608Metric, symbol Device:LED
- removed D98: OscTuneLED9, LED_SMD:LED_0603_1608Metric, symbol Device:LED
- removed D99: OscTuneLED10, LED_SMD:LED_0603_1608Metric, symbol Device:LED
- removed J1: DEBUG, Connector_PinHeader_1.27mm:PinHeader_2x05_P1.27mm_Vertical_SMD, symbol Connector_Generic:Conn_02x05_Odd_Even
- removed J15: USB_B_Micro, Connector_USB:USB_Micro-B_Amphenol_10118194_Horizontal, symbol Connector:USB_B_Micro
- removed J17: BT_DEBUG, Connector_PinHeader_1.27mm:PinHeader_2x05_P1.27mm_Vertical_SMD, symbol Connector_Generic:Conn_02x05_Odd_Even
- removed J2: MIDI IN, 5PINDIN:SWITCHCRAFT_57PC5F, symbol Connector:DIN-5_180degree
- removed J23: OLEDConn, TE FPC:TE_1-1734592-8, symbol 1-1734592-8:1-1734592-8-ELW2701AA
- removed J25: LeftI2C0Test, Connector_PinSocket_2.54mm:PinSocket_2x02_P2.54mm_Vertical, symbol Connector_Generic:Conn_01x04
- removed J29: LeftI2C1Test, Connector_PinSocket_2.54mm:PinSocket_2x02_P2.54mm_Vertical, symbol Connector_Generic:Conn_01x04
- removed J3: MIDI OUT, 5PINDIN:SWITCHCRAFT_57PC5F, symbol Connector:DIN-5_180degree
- removed J30: LeftI2C2Test, Connector_PinSocket_2.54mm:PinSocket_2x02_P2.54mm_Vertical, symbol Connector_Generic:Conn_01x04
- removed J31: LeftI2C3Test, Connector_PinSocket_2.54mm:PinSocket_2x02_P2.54mm_Vertical, symbol Connector_Generic:Conn_01x04
- removed J32: RightI2C0Test, Connector_PinSocket_2.54mm:PinSocket_2x02_P2.54mm_Vertical, symbol Connector_Generic:Conn_01x04
- removed J33: RightI2C1Test, Connector_PinSocket_2.54mm:PinSocket_2x02_P2.54mm_Vertical, symbol Connector_Generic:Conn_01x04
- removed J34: RightI2C2Test, Connector_PinSocket_2.54mm:PinSocket_2x02_P2.54mm_Vertical, symbol Connector_Generic:Conn_01x04
- removed J35: RightI2C3Test, Connector_PinSocket_2.54mm:PinSocket_2x02_P2.54mm_Vertical, symbol Connector_Generic:Conn_01x04
- removed J36: SPIBus1Test, Connector_PinHeader_2.54mm:PinHeader_2x03_P2.54mm_Vertical, symbol Connector_Generic:Conn_01x06
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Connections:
- no-connect marks 262 -> 55
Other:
- added sheet Bluetooth (Bluetooth.kicad_sch)
- added sheet DACs (DACs.kicad_sch)
- added sheet I2C Muxers (I2C_Muxers.kicad_sch)
- added sheet LEDs (LEDs.kicad_sch)
- added sheet MCU (MCU.kicad_sch)
- added sheet MIDI (MIDI.kicad_sch)
- added sheet OLED Display (OLED Display.kicad_sch)
- added sheet Switches (Switches.kicad_sch)
- added sheet USB (USB.kicad_sch)
- note removed: "LEFT0:00"
- note removed: "LEFT0:01"
- note removed: "LEFT0:10"
- note removed: "LEFT0:11"
- note removed: "LEFT1:00"
- note removed: "LEFT1:01"
- note removed: "LEFT1:10"
- note removed: "LEFT1:11"
- note removed: "LEFT3:00"
- note removed: "LEFT3:01"
- note removed: "LEFT3:10"
- note removed: "RIGHT1:00"
- note removed: "RIGHT1:01"
- note removed: "RIGHT1:10"
- note removed: "RIGHT2:00"
- note removed: "RIGHT2:01"
- note removed: "RIGHT2:10"
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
